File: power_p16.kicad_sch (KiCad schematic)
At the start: 21 parts, among them J1 LSHM-140-04.0-L-DV-A-N-K-TR, U1 LT8350S

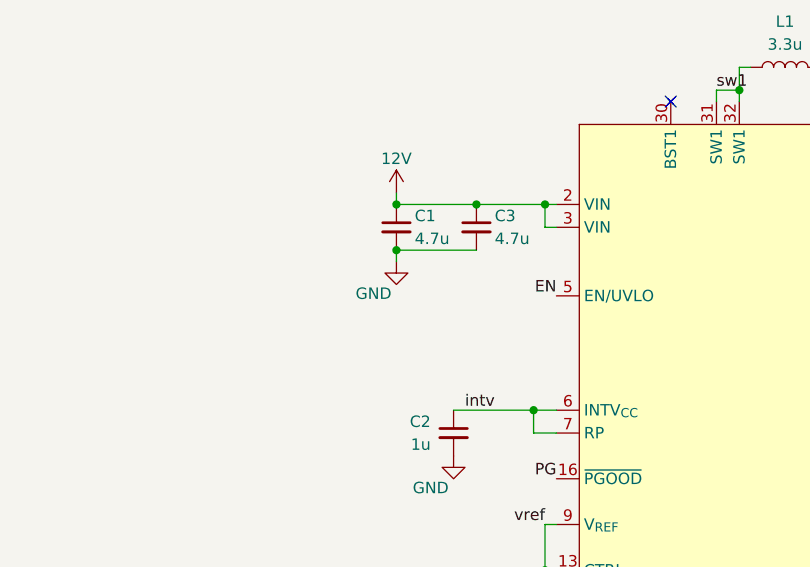
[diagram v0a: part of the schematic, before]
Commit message: Add input RC snubber
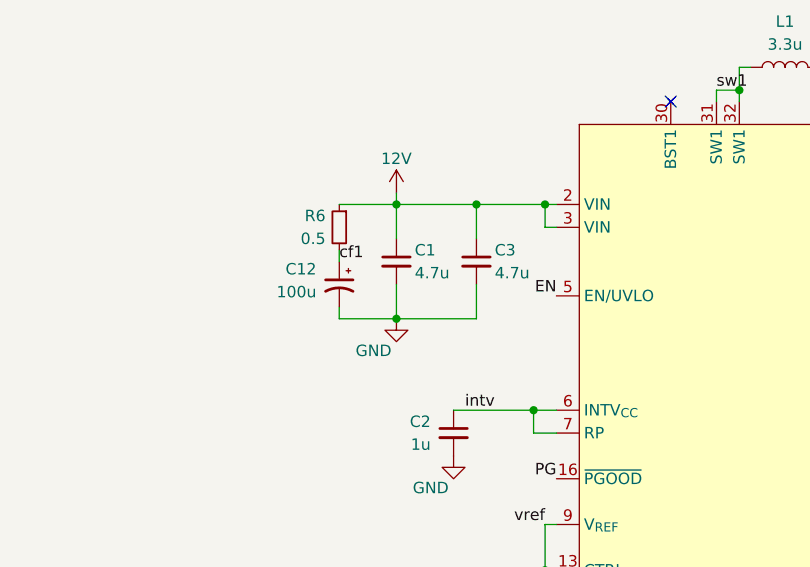
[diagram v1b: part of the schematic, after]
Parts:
- added C12: 100u, lib:T521X, symbol Device:C_Polarized_Small_US
- added R6: 0.5, Resistor_SMD:R_0603_1608Metric, symbol Device:R_Small
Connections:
- net 12V: now also R6.1
- net GND: now also C12.2
- new net cf1: C12.1, R6.2
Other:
- moved on the sheet: C1, C3

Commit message: update feedback resistor to thin film
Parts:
- R1: M Vishay -> Panasonic; MPN CRCW0603110KFKEA -> ERA-3AEB114V
- R2: M Vishay -> Panasonic; MPN CRCW06037K32FKTA -> ERA-3AEB7321V
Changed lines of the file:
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@@
 			)
 		)
-		(property "Description" "7.32 kOhms ±1% 0.1W, 1/10W Chip Resistor 0603 (1608 Metric) Automotive AEC-Q200 Thick Film"
+		(property "Description" "7.32 kOhms ±0.1% 0.1W, 1/10W Chip Resistor 0603 (1608 Metric) Automotive AEC-Q200 Thin Film"
 			(at 187.96 77.47 0)
 			(effects
@@
 			)
 		)
-		(property "M" "Vishay"
+		(property "M" "Panasonic"
 			(at 187.96 77.47 0)
 			(effects
@@
 			)
 		)
-		(property "MPN" "CRCW06037K32FKTA"
+		(property "MPN" "ERA-3AEB7321V"
 			(at 187.96 77.47 0)
 			(effects
@@
 			)
 		)
-		(property "Description" "110 kOhms ±1% 0.1W, 1/10W Chip Resistor 0603 (1608 Metric) Automotive AEC-Q200 Thick Film"
+		(property "Description" "110 kOhms ±0.1% 0.1W, 1/10W Chip Resistor 0603 (1608 Metric) Automotive AEC-Q200 Thin Film"
 			(at 187.96 64.77 0)
 			(effects
@@
 			)
 		)
-		(property "M" "Vishay"
+		(property "M" "Panasonic"
 			(at 187.96 64.77 0)
 			(effects
@@
 			)
 		)
-		(property "MPN" "CRCW0603110KFKEA"
+		(property "MPN" "ERA-3AEB114V"
 			(at 187.96 64.77 0)
 			(effects

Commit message: Update
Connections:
- net 16V: now also J1.62 (Pin_62), J1.64 (Pin_64), J1.66 (Pin_66), J1.68 (Pin_68), J1.70 (Pin_70); no longer J1.52 (Pin_52), J1.54 (Pin_54), J1.56 (Pin_56), J1.58 (Pin_58), J1.60 (Pin_60)
- net GND: now also J1.52 (Pin_52), J1.54 (Pin_54), J1.56 (Pin_56), J1.58 (Pin_58), J1.60 (Pin_60); no longer J1.62 (Pin_62), J1.64 (Pin_64), J1.66 (Pin_66), J1.68 (Pin_68), J1.70 (Pin_70)
